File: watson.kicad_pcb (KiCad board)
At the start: 2 copper layers, 84 x 30 mm, 51 parts, among them P1 CONN_1, P2 CONN_1, P3 CONN_1, P4 CONN_1, P5 BNC, P6 CONN_1, U1 78L05, U2 79L05, U3 AD8031, U4 AD603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

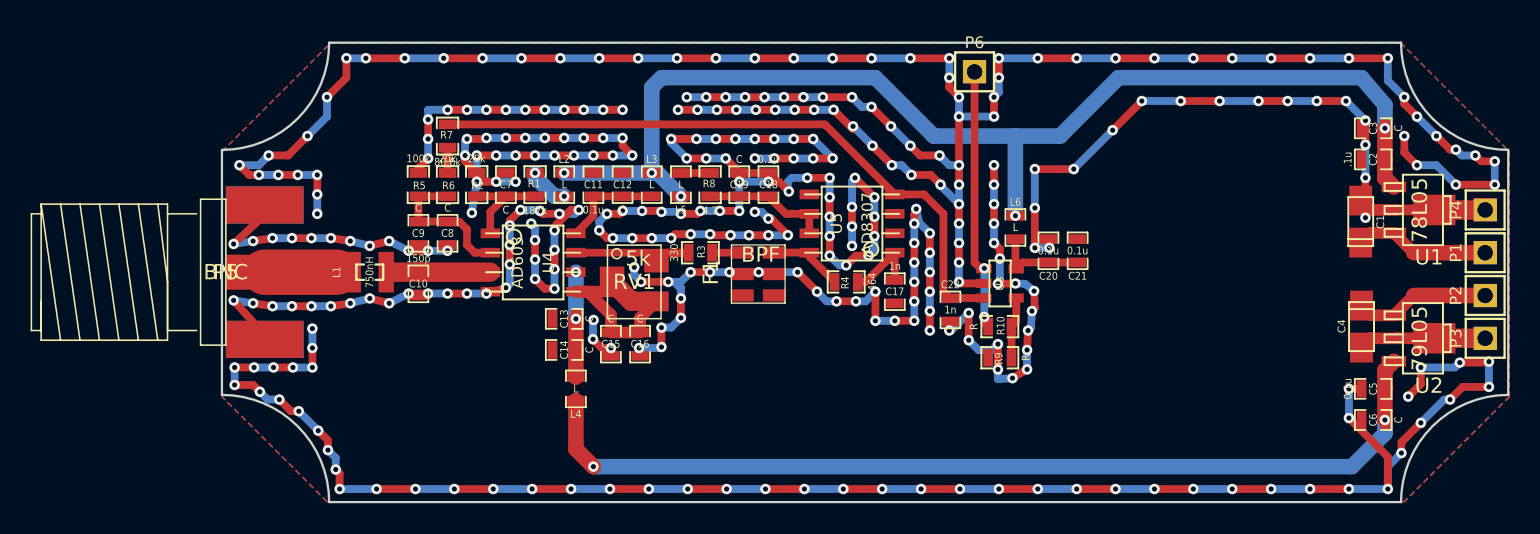
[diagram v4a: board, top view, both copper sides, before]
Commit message: I'm a terrible committer. I think these are the latest files that I actually sent to OSH Park... I hope....
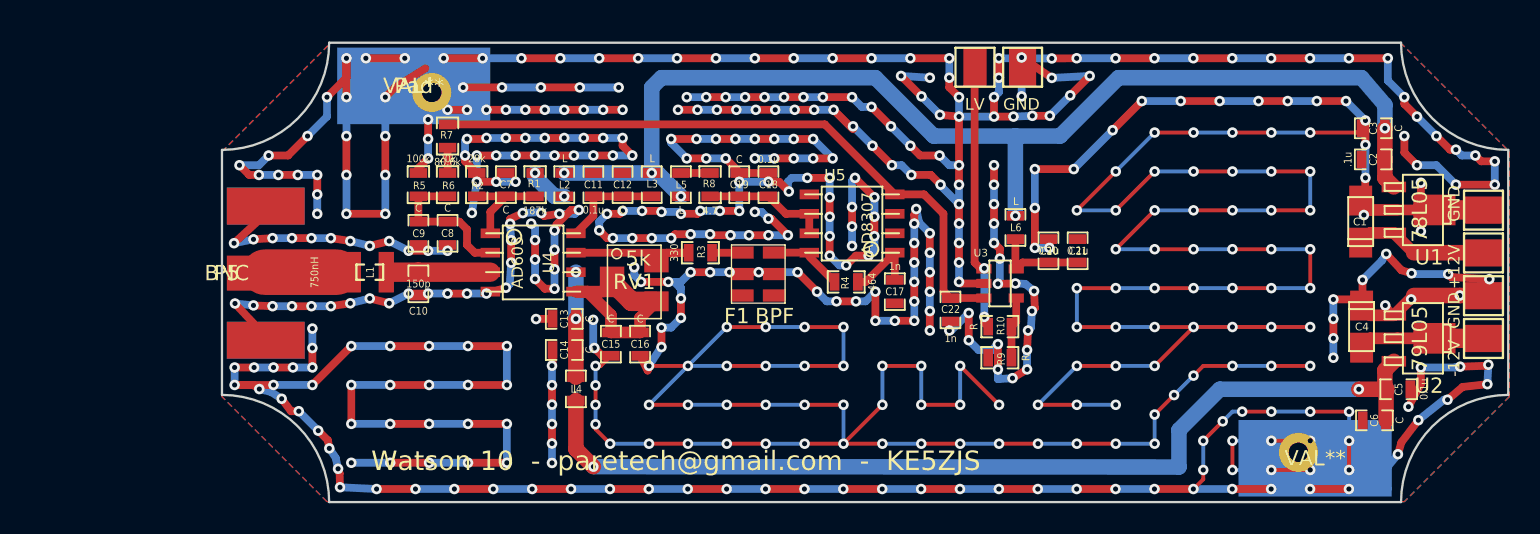
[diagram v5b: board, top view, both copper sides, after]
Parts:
- removed P4: CONN_1, PIN_ARRAY_1
- added ?: VAL**, hole, F.Cu at (225.2, 149.9)
- added ?: VAL**, Pad, F.Cu at (226.3, 150.3)
- added GND: CONN_1, PIN_ARRAY_1, F.Cu at (237.3, 134.1)
- added GND: Val**, PIN_ARRAY_1, F.Cu at (207.2, 124.8)
- added Pad: VAL**, Pad, F.Cu at (167.5, 126.0)
- added hole: VAL**, hole, F.Cu at (168.6, 126.4)
- moved C5 1.66 mm to (231.8, 145.8), turned to 180 degrees
- moved LV 0.31 mm to (204.1, 124.8)
- moved GND 0.11 mm to (237.3, 139.7)
- moved +12V 0.11 mm to (237.3, 136.9)
- moved -12V 0.11 mm to (237.3, 142.5)
- moved P5 0.09 mm to (155.3, 138.2)
- moved C6 0.08 mm to (230.2, 147.9)
- renumbered P1 to +12V, P3 to -12V, P2 to GND, P6 to LV
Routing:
- net GND: track 592.3 -> 1015.6 mm, vias 341 -> 514
- net (no net): track 3.21 -> 0.00 mm, vias 3 -> 0
- net -5V: track 62.3 -> 64.1 mm
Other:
- board text added: "Watson 10 - paretech@gmail.com - KE5ZJS"
